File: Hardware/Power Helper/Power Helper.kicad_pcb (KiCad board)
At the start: 2 copper layers, 54.3 x 27 mm, 15 parts, among them J1 USB_C_Receptacle_Power_Only, J2 Conn_02x02_Odd_Even, J3 Conn_02x02_Odd_Even, SW1 SW_SPDT, SW2 SW_SPDT, SW3 SW_SPDT, U1 AZ1117-3.3

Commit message: Add LED helper
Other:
- board text removed: "JLCJLCJLCJLC"

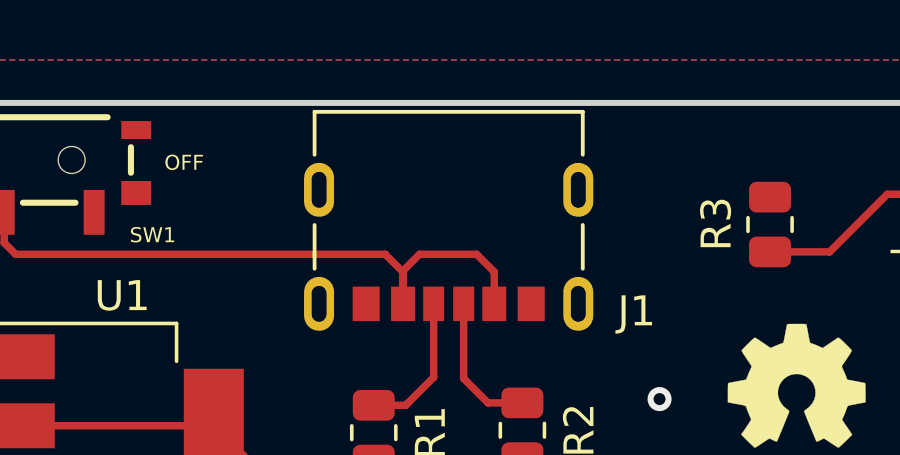
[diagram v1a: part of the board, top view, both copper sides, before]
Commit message: JLC fix
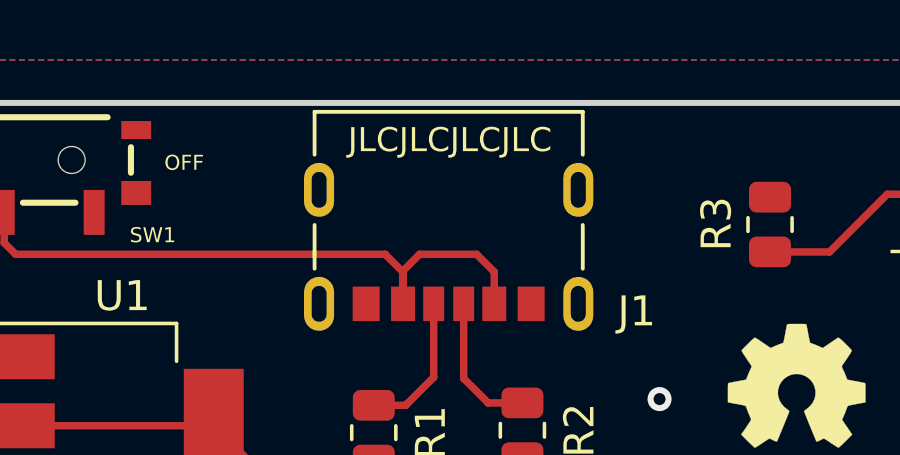
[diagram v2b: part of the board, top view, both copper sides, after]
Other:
- board text added: "JLCJLCJLCJLC"
